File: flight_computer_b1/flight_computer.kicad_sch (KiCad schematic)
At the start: 9 parts, among them J1 Pi Connector, J2 Conn_01x03, J3 Conn_02x02_Odd_Even, J4 DB25_Socket, J5 DB25_Socket

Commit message: flight computer changes
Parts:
- J4: footprint Connector_Dsub:DSUB-25_Socket_Horizontal_P2.77x2.84mm_EdgePinOffset4.94mm_Housed_MountingHolesOffset4.94mm -> Connector_Dsub:DSUB-25_Socket_Vertical_P2.77x2.84mm_MountingHoles
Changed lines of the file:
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@@
 			)
 		)
-		(property "Footprint" "Connector_Dsub:DSUB-25_Socket_Horizontal_P2.77x2.84mm_EdgePinOffset4.94mm_Housed_MountingHolesOffset4.94mm"
+		(property "Footprint" "Connector_Dsub:DSUB-25_Socket_Vertical_P2.77x2.84mm_MountingHoles"
 			(at 205.74 97.79 0)
 			(effects

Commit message: flight computer updates
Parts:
- renumbered J3 to J2, J2 to J3
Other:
- added sheet rs485 (rs485.kicad_sch)
- moved on the sheet: J1, J2, J3, J4, J5, NT1, NT2, NT3, NT4

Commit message: flight computer changes
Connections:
- net RS485_UART_RX: now reaches J1.10 (Pin_10)
- net RS485_UART_TX: now reaches J1.8 (Pin_8)
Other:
- moved on the sheet: J1, J2, J3, J4, J5, NT1, NT2, NT3, NT4

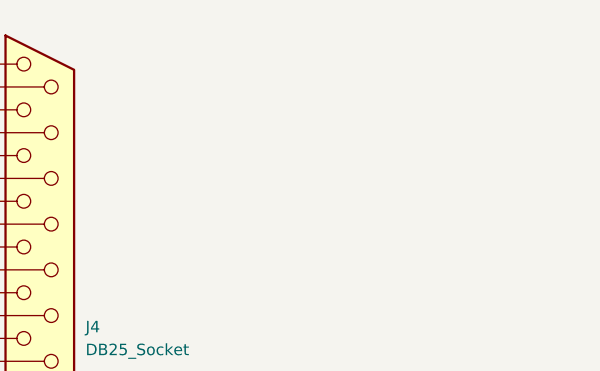
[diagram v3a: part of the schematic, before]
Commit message: flight computer layout changes
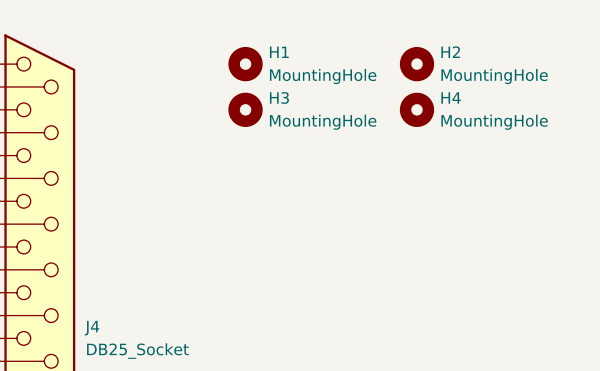
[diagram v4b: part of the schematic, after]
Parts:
- added H1, H2, H3, H4: MountingHole, MountingHole:MountingHole_2.7mm_M2.5, symbol Mechanical:MountingHole

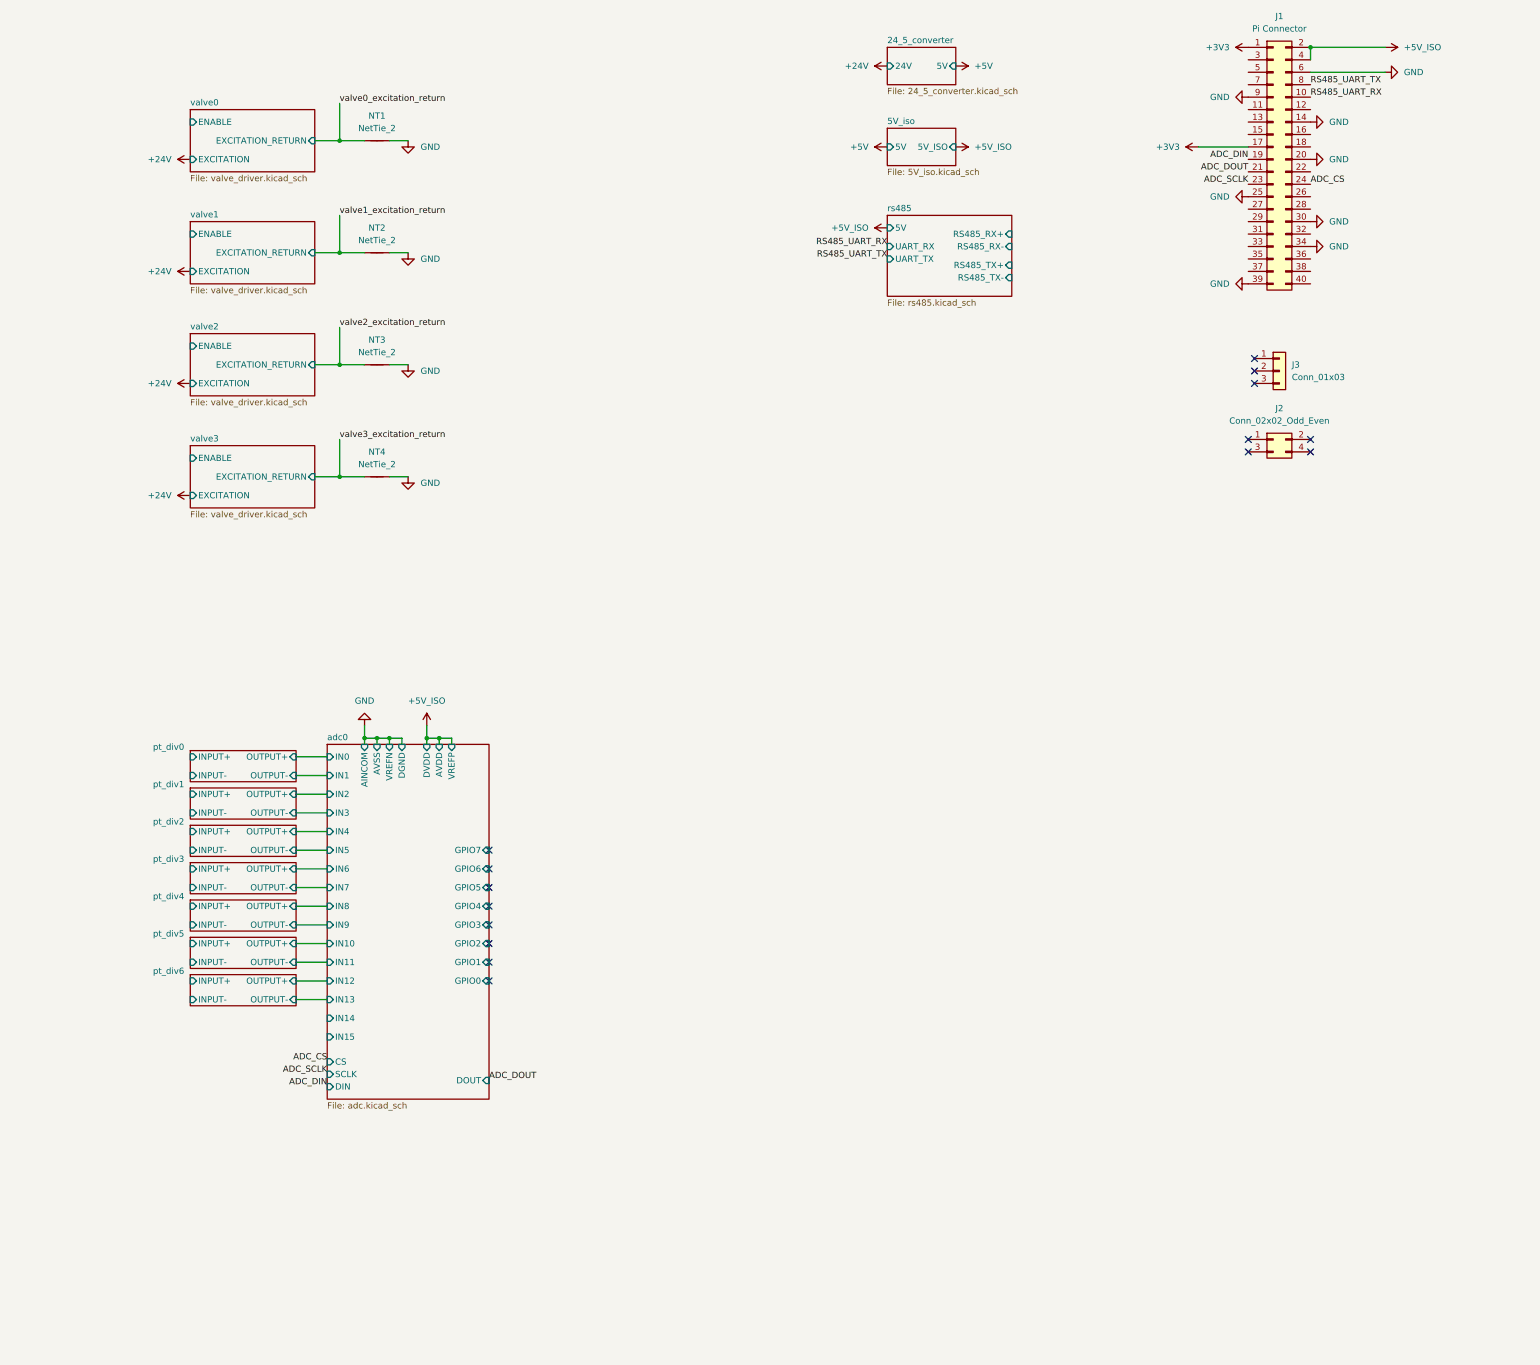
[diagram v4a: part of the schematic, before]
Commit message: flight computer: added mux and voltage sense channels
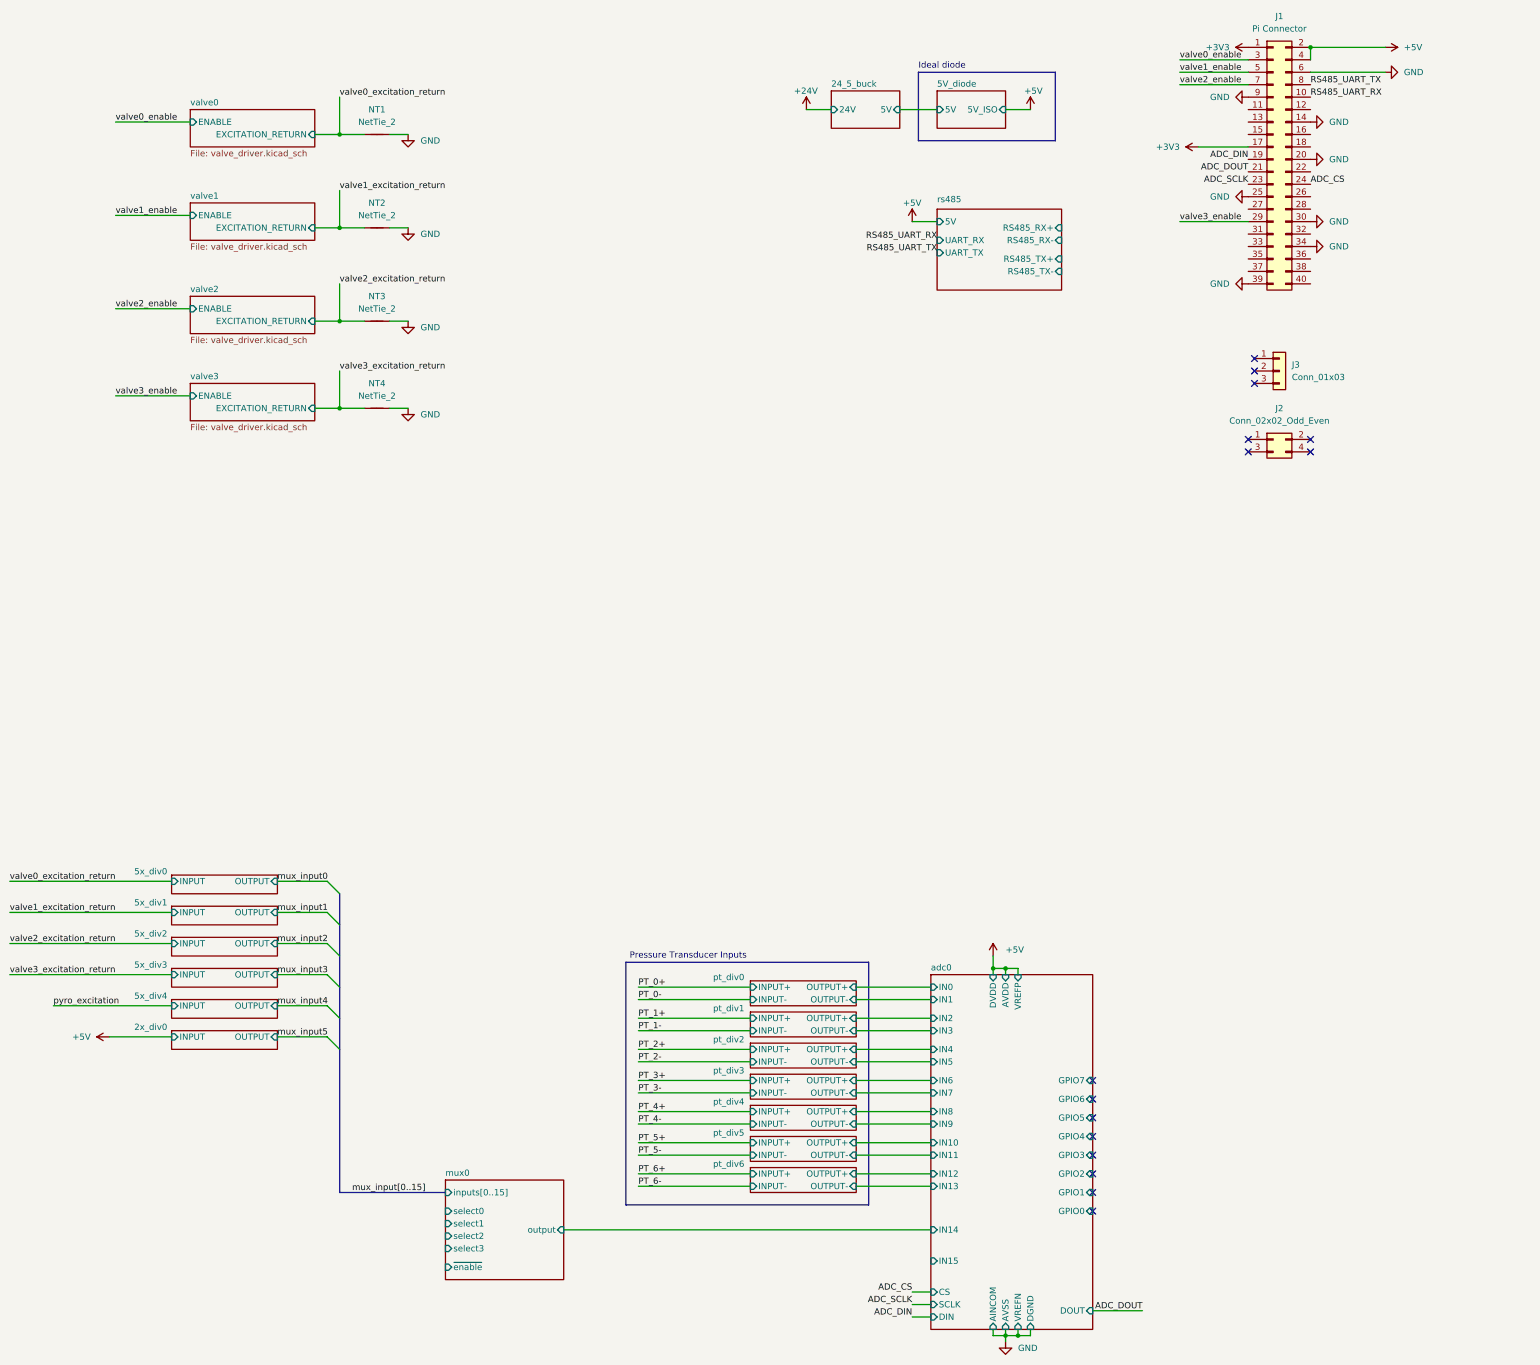
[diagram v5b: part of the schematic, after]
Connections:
- net +5V_ISO is gone; now on net +5V: J1.2 (Pin_2), J1.4 (Pin_4)
- net valve3_enable: now reaches J1.29 (Pin_29)
- net valve0_enable: now reaches J1.3 (Pin_3)
- net valve1_enable: now reaches J1.5 (Pin_5)
- net valve2_enable: now reaches J1.7 (Pin_7)
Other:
- sheet 24_5_converter renamed 24_5_buck
- sheet 5V_iso renamed 5V_diode
- added sheet 2x_div0 (2x_div.kicad_sch)
- added sheet 5x_div0 (5x_div.kicad_sch)
- added sheet 5x_div1 (5x_div.kicad_sch)
- added sheet 5x_div2 (5x_div.kicad_sch)
- added sheet 5x_div3 (5x_div.kicad_sch)
- added sheet 5x_div4 (5x_div.kicad_sch)
- added sheet mux0 (mux.kicad_sch)
- sheet 24_5_buck: file 24_5_converter.kicad_sch -> 24_5_buck.kicad_sch
- sheet valve0 ports: added none; removed EXCITATION
- sheet valve1 ports: added none; removed EXCITATION
- sheet valve2 ports: added none; removed EXCITATION
- sheet valve3 ports: added none; removed EXCITATION
- note added: "Ideal diode"
- note added: "Pressure Transducer Inputs"
- company: (none) -> Purdue Space Program Liquids
- moved on the sheet: NT1, NT2, NT3, NT4

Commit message: flight computer: added pyro circuit and digikey part numbers
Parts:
- removed NT1, NT2, NT3, NT4: NetTie_2, symbol Device:NetTie_2
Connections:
- net PYRO_FIRE: now reaches J1.16 (Pin_16)
- net PYRO_ARM: now reaches J1.18 (Pin_18)
- net mux_addr0: now reaches J1.31 (Pin_31)
- net mux_addr1: now reaches J1.33 (Pin_33)
- net mux_addr2: now reaches J1.35 (Pin_35)
- net mux_addr3: now reaches J1.37 (Pin_37)
- no-connect marks 15 -> 84
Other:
- added sheet pyro0 (pyro.kicad_sch)
- sheet rs485 ports: added none; removed 5V
- note added: "Connectors"
- note added: "Power"
- note added: "Power Sources/Sinks"
- moved on the sheet: H1, H2, H3, H4, J1, J2, J3, J4, J5

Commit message: flight computer: new ideal diode, small schematic changes
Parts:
- added NT1: NetTie_2, symbol Device:NetTie_2
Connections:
- net GND: now also NT1.2
- net PT_0+: now also J4.3
- net PT_0-: now also J4.4
- net PT_1+: now also J4.7
- net PT_1-: now also J4.8
- net PT_2+: now also J4.9
- net PT_2-: now also J4.10
- net PT_3+: now also J4.11
- net PT_3-: now also J4.12
- net PT_4+: now also J4.13
- net PT_4-: now also J4.14 (P14)
- net pyro_excitation_return: now also J4.16 (P16)
- net valve0_excitation_return: now also J4.18 (P18)
- net valve1_excitation_return: now also J4.20 (P20)
- net pyro_excitation: now reaches J4.15 (P15)
- net valve0_excitation: now reaches J4.17 (P17)
- net valve1_excitation: now reaches J4.19 (P19)
- new net PT_GND: NT1.1
- no-connect marks 84 -> 58
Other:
- removed sheet 5x_div0
- removed sheet 5x_div1
- removed sheet 5x_div2
- removed sheet 5x_div3
- removed sheet 5x_div4
- sheet 5V_diode ports: added +5V_ISO; removed 5V_ISO
- sheet pyro0 ports: added CONTINUITY; removed none
- sheet valve0 ports: added CONTINUITY, EXCITATION; removed none
- sheet valve1 ports: added CONTINUITY, EXCITATION; removed none
- sheet valve2 ports: added CONTINUITY, EXCITATION; removed none
- sheet valve3 ports: added CONTINUITY, EXCITATION; removed none

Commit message: flight computer: routing updates
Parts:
- added J4: Screw_Terminal_01x02, avi_lib:PHOENIX_1935776, symbol Connector:Screw_Terminal_01x02
- renumbered H3 to H2, H2 to H3, J5 to J1, J4 to J2, J1 to J5, J2 to J6
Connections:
- net +24V: now also J1.20 (P20), J2.1, J4.1 (Pin_1)
- net GND: now also J4.2 (Pin_2)
- net PT_1+: now also J2.5; no longer J2.7
- net PT_1-: now also J2.6; no longer J2.8
- net PT_2+: now also J2.7; no longer J2.9
- net PT_2-: now also J2.8; no longer J2.10
- net PT_3+: now also J2.9; no longer J2.11
- net PT_3-: now also J2.10; no longer J2.12
- net PT_4+: now also J2.11; no longer J2.13
- net PT_4-: now also J2.12; no longer J2.14 (P14)
- net PT_5+: now also J1.22 (P22)
- net PT_5-: now also J1.23 (P23)
- net PT_6+: now also J1.24 (P24)
- net PT_6-: now also J1.25 (P25)
- net PT_GND: now also J1.21 (P21), J2.2
- net valve2_excitation: now also J2.21 (P21)
- net valve2_excitation_return: now also J2.22 (P22)
- net valve3_excitation: now also J2.23 (P23)
- net valve3_excitation_return: now also J2.24 (P24)
- net ESC_RX-: now reaches J1.10
- net ESC_TX+: now reaches J1.11
- net ESC_TX-: now reaches J1.12
- net ESC_RX+: now reaches J1.9
- no-connect marks 58 -> 46
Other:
- sheet adc0 ports: added VDD, VSS; removed AVDD, AVSS, DGND, DVDD
- sheet mux0 ports: added OUTPUT; removed output, ~{enable}
- note added: "https://www.digikey.com/en/products/detail/nxp-usa-inc/TJA1051T-3-1J/5035822"
